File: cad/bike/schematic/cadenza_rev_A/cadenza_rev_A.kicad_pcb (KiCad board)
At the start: 2 copper layers, 80 x 50 mm, 35 parts, among them J2 USB_C_Receptacle, J3 Conn_01x02, Q1 BC547, U1 TLC5916, U10 HDSP-A151, U11 TLC5916, U12 HDSP-A151, U13 STM32F105RCTx, U14 INA193, U15 TLC5916, U2 HDSP-A151, U3 TLC5916, U4 HDSP-A151, U5 TLC5916, U6 HDSP-A151, U7 TLC5916, U8 HDSP-A151, U9 TLC5916

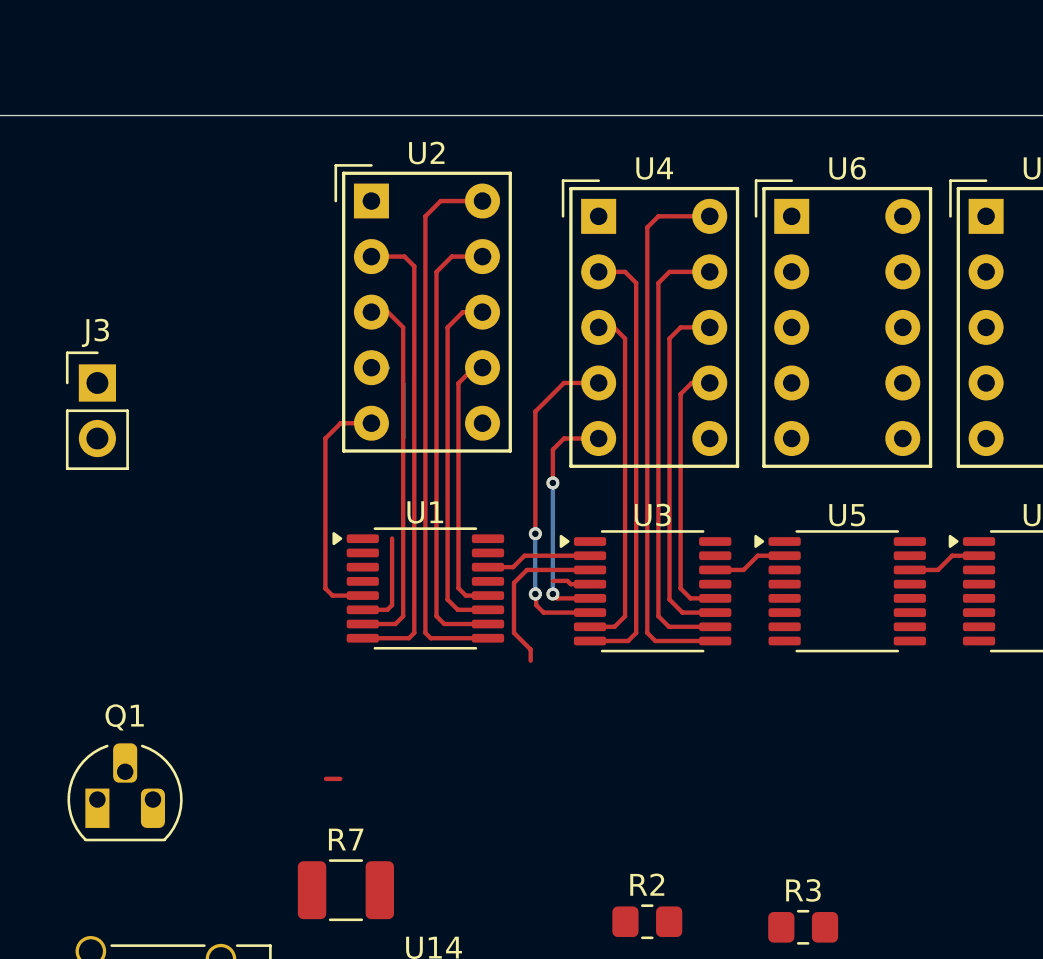
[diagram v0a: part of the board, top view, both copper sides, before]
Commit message: new placement for the LED chips
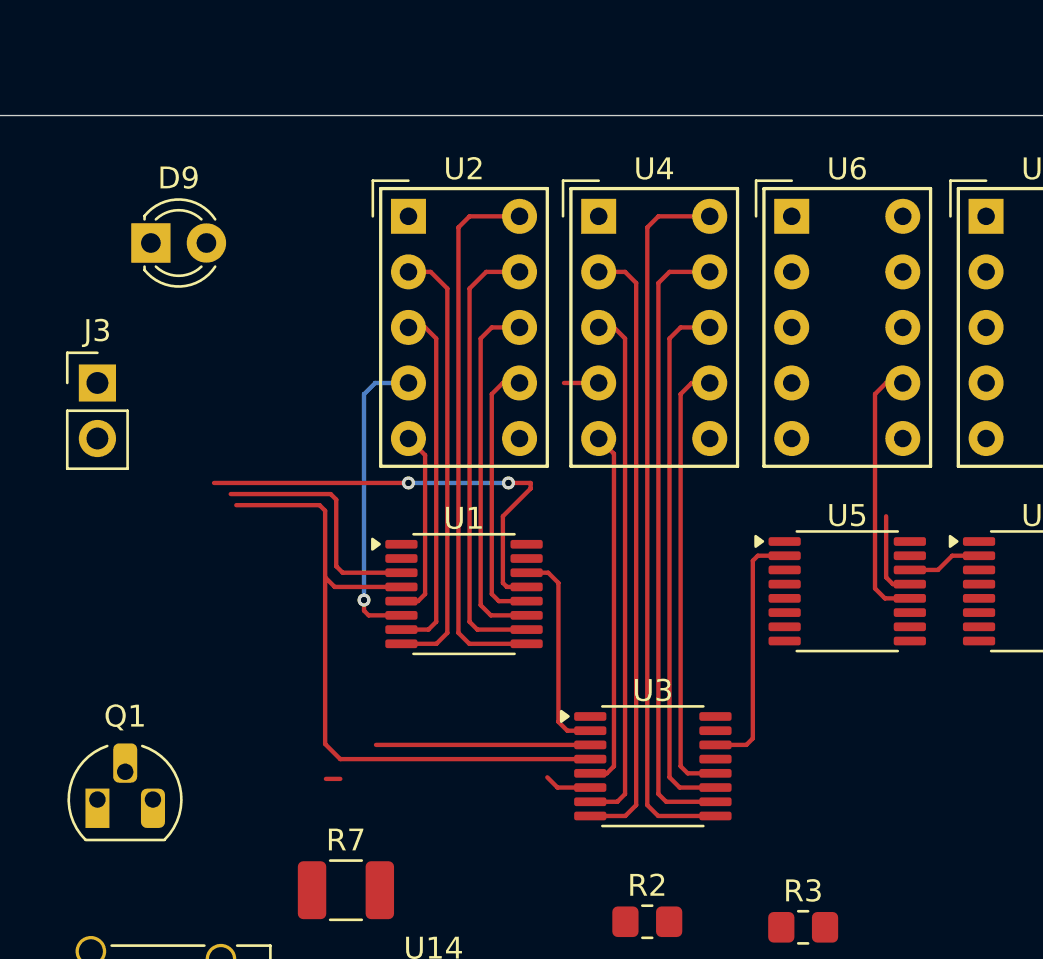
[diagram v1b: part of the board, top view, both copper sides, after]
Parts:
- added D9: LED, LED_THT:LED_D3.0mm, F.Cu at (57.1, 55.8)
- moved U3 8.00 mm to (80.0, 79.8)
- moved U2 1.83 mm to (68.8, 54.6)
- moved U1 1.78 mm to (71.4, 71.9)
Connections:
- U5 pad 10: unconnected-(U5-~{OUT5}-Pad10) -> Net-(U5-~{OUT5})
- U5 pad 11: unconnected-(U5-~{OUT6}-Pad11) -> Net-(U5-~{OUT6})
- U5 pad 12: unconnected-(U5-~{OUT7}-Pad12) -> Net-(U5-~{OUT7})
- U6 pad 7: unconnected-(U6-DP-Pad7) -> Net-(U5-~{OUT7})
- U6 pad 8: unconnected-(U6-C-Pad8) -> Net-(U5-~{OUT6})
- U6 pad 9: unconnected-(U6-B-Pad9) -> Net-(U5-~{OUT5})
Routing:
- net Net-(U1-LE(ED1)): track 1.76 -> 30.9 mm
- net Net-(U1-~{OE}(ED2)): track 0.00 -> 24.7 mm, vias 0 -> 2
- net Net-(U1-CLK): track 7.60 -> 20.9 mm
- net Net-(U5-~{OUT7}): track 0.00 -> 12.2 mm
- net Net-(U3-~{OUT1}): track 15.0 -> 3.74 mm, vias 2 -> 0
- net Net-(U3-~{OUT7}): track 12.2 -> 20.3 mm
- net Net-(U3-~{OUT5}): track 20.6 -> 28.7 mm
- net Net-(U3-~{OUT6}): track 16.3 -> 24.4 mm
- net Net-(U3-~{OUT2}): track 15.9 -> 24.0 mm
- net Net-(U3-SDO): track 3.44 -> 11.5 mm
- net Net-(U3-~{OUT4}): track 24.9 -> 32.8 mm
- net Net-(U3-~{OUT3}): track 20.2 -> 28.1 mm
- net Net-(U1-~{OUT1}): track 7.77 -> 13.9 mm, vias 0 -> 1
- net Net-(U3-~{OUT0}): track 10.7 -> 16.5 mm, vias 2 -> 0
- net Net-(U1-SDO): track 4.88 -> 9.62 mm
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
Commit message: routing progress update
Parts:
- added C3: 100nF, Capacitor_SMD:C_0805_2012Metric_Pad1.18x1.45mm_HandSolder, F.Cu at (77.0, 71.2)
- added C4: 100nF, Capacitor_SMD:C_0805_2012Metric_Pad1.18x1.45mm_HandSolder, F.Cu at (83.1, 74.9)
- added C5: 100nF, Capacitor_SMD:C_0805_2012Metric_Pad1.18x1.45mm_HandSolder, F.Cu at (94.2, 70.9)
- added C6: 100nF, Capacitor_SMD:C_0805_2012Metric_Pad1.18x1.45mm_HandSolder, F.Cu at (100.8, 74.9)
- added R10: R_US, Resistor_SMD:R_0805_2012Metric_Pad1.20x1.40mm_HandSolder, F.Cu at (102.4, 92.7)
- added R8: R_US, Resistor_SMD:R_0805_2012Metric_Pad1.20x1.40mm_HandSolder, F.Cu at (96.6, 87.3)
- added R9: R_US, Resistor_SMD:R_0805_2012Metric_Pad1.20x1.40mm_HandSolder, F.Cu at (91.2, 93.2)
- moved U15 87.8 mm to (116.5, 79.1)
- moved R1 32.0 mm to (71.4, 76.2), turned to 180 degrees
- moved R2 9.66 mm to (87.6, 81.3)
- moved U7 8.00 mm to (97.8, 79.8)
- moved R4 4.66 mm to (108.7, 78.5)
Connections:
- U1 pad 2: unconnected-(U1-SDI-Pad2) -> Net-(U1-SDI)
- U11 pad 15: unconnected-(U11-R-EXT-Pad15) -> Net-(U11-R-EXT)
- U13 pad 14: unconnected-(U13-PA0-Pad14) -> Net-(U1-SDI)
- U5 pad 5: unconnected-(U5-~{OUT0}-Pad5) -> Net-(U5-~{OUT0})
- U5 pad 6: unconnected-(U5-~{OUT1}-Pad6) -> Net-(U5-~{OUT1})
- U5 pad 7: unconnected-(U5-~{OUT2}-Pad7) -> Net-(U5-~{OUT2})
- U5 pad 8: unconnected-(U5-~{OUT3}-Pad8) -> Net-(U5-~{OUT3})
- U5 pad 9: unconnected-(U5-~{OUT4}-Pad9) -> Net-(U5-~{OUT4})
- U6 pad 10: unconnected-(U6-A-Pad10) -> Net-(U5-~{OUT4})
- U6 pad 2: unconnected-(U6-F-Pad2) -> Net-(U5-~{OUT3})
- U6 pad 3: unconnected-(U6-G-Pad3) -> Net-(U5-~{OUT2})
- U6 pad 4: unconnected-(U6-E-Pad4) -> Net-(U5-~{OUT1})
- U6 pad 5: unconnected-(U6-D-Pad5) -> Net-(U5-~{OUT0})
- U7 pad 10: unconnected-(U7-~{OUT5}-Pad10) -> Net-(U7-~{OUT5})
- U7 pad 11: unconnected-(U7-~{OUT6}-Pad11) -> Net-(U7-~{OUT6})
- U7 pad 12: unconnected-(U7-~{OUT7}-Pad12) -> Net-(U7-~{OUT7})
- U7 pad 15: unconnected-(U7-R-EXT-Pad15) -> Net-(U7-R-EXT)
- U7 pad 5: unconnected-(U7-~{OUT0}-Pad5) -> Net-(U7-~{OUT0})
- U7 pad 6: unconnected-(U7-~{OUT1}-Pad6) -> Net-(U7-~{OUT1})
- U7 pad 7: unconnected-(U7-~{OUT2}-Pad7) -> Net-(U7-~{OUT2})
- U7 pad 8: unconnected-(U7-~{OUT3}-Pad8) -> Net-(U7-~{OUT3})
- U7 pad 9: unconnected-(U7-~{OUT4}-Pad9) -> Net-(U7-~{OUT4})
- U8 pad 10: unconnected-(U8-A-Pad10) -> Net-(U7-~{OUT4})
- U8 pad 2: unconnected-(U8-F-Pad2) -> Net-(U7-~{OUT3})
- U8 pad 3: unconnected-(U8-G-Pad3) -> Net-(U7-~{OUT2})
- U8 pad 4: unconnected-(U8-E-Pad4) -> Net-(U7-~{OUT1})
- U8 pad 5: unconnected-(U8-D-Pad5) -> Net-(U7-~{OUT0})
- U8 pad 7: unconnected-(U8-DP-Pad7) -> Net-(U7-~{OUT7})
- U8 pad 8: unconnected-(U8-C-Pad8) -> Net-(U7-~{OUT6})
- U8 pad 9: unconnected-(U8-B-Pad9) -> Net-(U7-~{OUT5})
- U9 pad 15: unconnected-(U9-R-EXT-Pad15) -> Net-(U9-R-EXT)
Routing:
- net +5VL: track 0.00 -> 195.5 mm
- net Net-(U1-CLK): track 20.9 -> 65.1 mm, vias 0 -> 5
- net Net-(U7-~{OUT4}): track 0.00 -> 32.7 mm
- net Net-(U7-~{OUT5}): track 0.00 -> 28.6 mm
- net Net-(U7-~{OUT3}): track 0.00 -> 28.2 mm
- net Net-(U1-~{OE}(ED2)): track 24.7 -> 52.6 mm, vias 2 -> 6
- net Net-(U5-~{OUT4}): track 0.00 -> 24.8 mm
- net Net-(U7-~{OUT6}): track 0.00 -> 24.3 mm
- net Net-(U7-~{OUT2}): track 0.00 -> 24.0 mm
- net +3.3V: track 0.00 -> 21.8 mm, vias 0 -> 1
- net Net-(U5-~{OUT5}): track 0.00 -> 20.7 mm
- net Net-(U5-~{OUT3}): track 0.00 -> 20.2 mm
- net Net-(U7-~{OUT7}): track 0.00 -> 20.1 mm
- net Net-(U3-~{OUT1}): track 3.74 -> 21.4 mm, vias 0 -> 2
- net Net-(U7-~{OUT0}): track 0.00 -> 16.5 mm
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
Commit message: routing progress update
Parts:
- added C7: 100nF, Capacitor_SMD:C_0805_2012Metric_Pad1.18x1.45mm_HandSolder, F.Cu at (118.6, 74.9)
- added C8: 100nF, Capacitor_SMD:C_0805_2012Metric_Pad1.18x1.45mm_HandSolder, F.Cu at (112.0, 70.9)
- moved R4 55.5 mm to (53.3, 74.2), turned to 180 degrees
- moved R9 23.0 mm to (106.7, 76.2), turned to 180 degrees
- moved U13 18.1 mm to (95.0, 93.2)
- moved R10 15.8 mm to (115.6, 84.1), turned to 180 degrees
- moved U15 14.2 mm to (116.6, 93.2)
- moved R3 11.1 mm to (88.9, 76.2), turned to 180 degrees
- moved R2 8.12 mm to (80.0, 84.1), turned to 180 degrees
- moved U11 8.00 mm to (115.6, 79.8)
- moved R8 3.47 mm to (97.8, 84.1), turned to 180 degrees
- moved C3 0.45 mm to (76.7, 70.9)
- moved U5 0.13 mm to (88.9, 71.9)
- moved U9 0.13 mm to (106.7, 71.9)
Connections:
- C6 pad 1: unconnected-(C6-Pad1) -> GND
- U10 pad 10: unconnected-(U10-A-Pad10) -> Net-(U10-A)
- U10 pad 2: unconnected-(U10-F-Pad2) -> Net-(U10-F)
- U10 pad 3: unconnected-(U10-G-Pad3) -> Net-(U10-G)
- U10 pad 4: unconnected-(U10-E-Pad4) -> Net-(U10-E)
- U10 pad 5: unconnected-(U10-D-Pad5) -> Net-(U10-D)
- U10 pad 7: unconnected-(U10-DP-Pad7) -> Net-(U10-DP)
- U10 pad 8: unconnected-(U10-C-Pad8) -> Net-(U10-C)
- U10 pad 9: unconnected-(U10-B-Pad9) -> Net-(U10-B)
- U11 pad 10: unconnected-(U11-~{OUT5}-Pad10) -> Net-(U11-~{OUT5})
- U11 pad 11: unconnected-(U11-~{OUT6}-Pad11) -> Net-(U11-~{OUT6})
- U11 pad 12: unconnected-(U11-~{OUT7}-Pad12) -> Net-(U11-~{OUT7})
- U11 pad 5: unconnected-(U11-~{OUT0}-Pad5) -> Net-(U11-~{OUT0})
- U11 pad 6: unconnected-(U11-~{OUT1}-Pad6) -> Net-(U11-~{OUT1})
- U11 pad 7: unconnected-(U11-~{OUT2}-Pad7) -> Net-(U11-~{OUT2})
- U11 pad 8: unconnected-(U11-~{OUT3}-Pad8) -> Net-(U11-~{OUT3})
- U11 pad 9: unconnected-(U11-~{OUT4}-Pad9) -> Net-(U11-~{OUT4})
- U12 pad 10: unconnected-(U12-A-Pad10) -> Net-(U11-~{OUT4})
- U12 pad 2: unconnected-(U12-F-Pad2) -> Net-(U11-~{OUT3})
- U12 pad 3: unconnected-(U12-G-Pad3) -> Net-(U11-~{OUT2})
- U12 pad 4: unconnected-(U12-E-Pad4) -> Net-(U11-~{OUT1})
- U12 pad 5: unconnected-(U12-D-Pad5) -> Net-(U11-~{OUT0})
- U12 pad 7: unconnected-(U12-DP-Pad7) -> Net-(U11-~{OUT7})
- U12 pad 8: unconnected-(U12-C-Pad8) -> Net-(U11-~{OUT6})
- U12 pad 9: unconnected-(U12-B-Pad9) -> Net-(U11-~{OUT5})
- U9 pad 10: unconnected-(U9-~{OUT5}-Pad10) -> Net-(U10-B)
- U9 pad 11: unconnected-(U9-~{OUT6}-Pad11) -> Net-(U10-C)
- U9 pad 12: unconnected-(U9-~{OUT7}-Pad12) -> Net-(U10-DP)
- U9 pad 5: unconnected-(U9-~{OUT0}-Pad5) -> Net-(U10-D)
- U9 pad 6: unconnected-(U9-~{OUT1}-Pad6) -> Net-(U10-E)
- U9 pad 7: unconnected-(U9-~{OUT2}-Pad7) -> Net-(U10-G)
- U9 pad 8: unconnected-(U9-~{OUT3}-Pad8) -> Net-(U10-F)
- U9 pad 9: unconnected-(U9-~{OUT4}-Pad9) -> Net-(U10-A)
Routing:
- net Net-(U1-LE(ED1)): track 19.9 -> 65.5 mm, vias 0 -> 2
- net +3.3V: track 21.8 -> 64.3 mm, vias 1 -> 5
- net Net-(U1-CLK): track 65.1 -> 102.9 mm, vias 5 -> 10
- net Net-(U11-~{OUT4}): track 0.00 -> 32.7 mm
- net Net-(U11-~{OUT5}): track 0.00 -> 28.6 mm
- net Net-(U11-~{OUT3}): track 0.00 -> 28.2 mm
- net Net-(U7-~{OUT1}): track 0.00 -> 26.6 mm, vias 0 -> 1
- net Net-(U11-~{OUT1}): track 0.00 -> 25.6 mm, vias 0 -> 1
- net Net-(U10-A): track 0.00 -> 24.9 mm
- net Net-(U11-~{OUT6}): track 0.00 -> 24.3 mm
- net Net-(U11-~{OUT2}): track 0.00 -> 24.0 mm
- net Net-(U10-B): track 0.00 -> 20.7 mm
- net Net-(U10-F): track 0.00 -> 20.3 mm
- net Net-(U11-~{OUT7}): track 0.00 -> 20.2 mm
- net Net-(U10-C): track 0.00 -> 16.6 mm
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
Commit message: added the SPI interface
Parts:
- added C10: 100nF, Capacitor_SMD:C_0805_2012Metric_Pad1.18x1.45mm_HandSolder, F.Cu at (81.4, 92.9)
- added C11: 100nF, Capacitor_SMD:C_0805_2012Metric_Pad1.18x1.45mm_HandSolder, F.Cu at (81.4, 95.9)
- added C9: 100nF, Capacitor_SMD:C_0805_2012Metric_Pad1.18x1.45mm_HandSolder, F.Cu at (81.4, 89.9)
- moved U13 1.63 mm to (93.7, 92.2), turned to -90 degrees
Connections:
- U1 pad 2: Net-(U1-SDI) -> /SPI_MOSI
- U1 pad 3: Net-(U1-CLK) -> /SPI_CLK
- U11 pad 3: Net-(U1-CLK) -> /SPI_CLK
- U13 pad 14: Net-(U1-SDI) -> unconnected-(U13-PA0-Pad14)
- U13 pad 21: unconnected-(U13-PA5-Pad21) -> /SPI_CLK
- U13 pad 22: unconnected-(U13-PA6-Pad22) -> /SPI_MISO
- U13 pad 23: unconnected-(U13-PA7-Pad23) -> /SPI_MOSI
- U15 pad 3: Net-(U1-CLK) -> /SPI_CLK
- U3 pad 3: Net-(U1-CLK) -> /SPI_CLK
- U5 pad 3: Net-(U1-CLK) -> /SPI_CLK
- U7 pad 3: Net-(U1-CLK) -> /SPI_CLK
- U9 pad 3: Net-(U1-CLK) -> /SPI_CLK
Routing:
- net Net-(U1-CLK): track 102.9 -> 0.00 mm, vias 10 -> 0
- net /SPI_CLK: track 0.00 -> 102.9 mm, vias 0 -> 10
- net Net-(U1-SDI): track 2.32 -> 0.00 mm
- net /SPI_MOSI: track 0.00 -> 2.32 mm

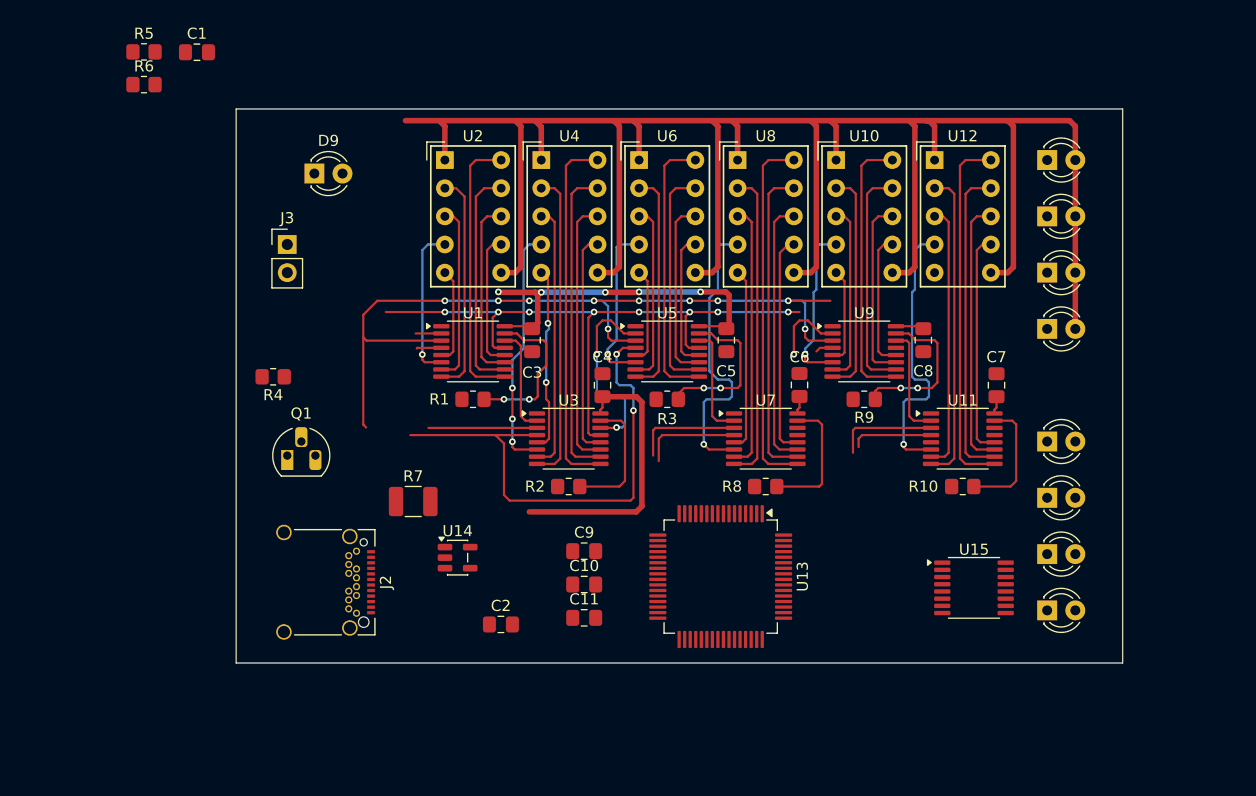
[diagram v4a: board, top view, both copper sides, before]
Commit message: added routing for the acceleration LEDs
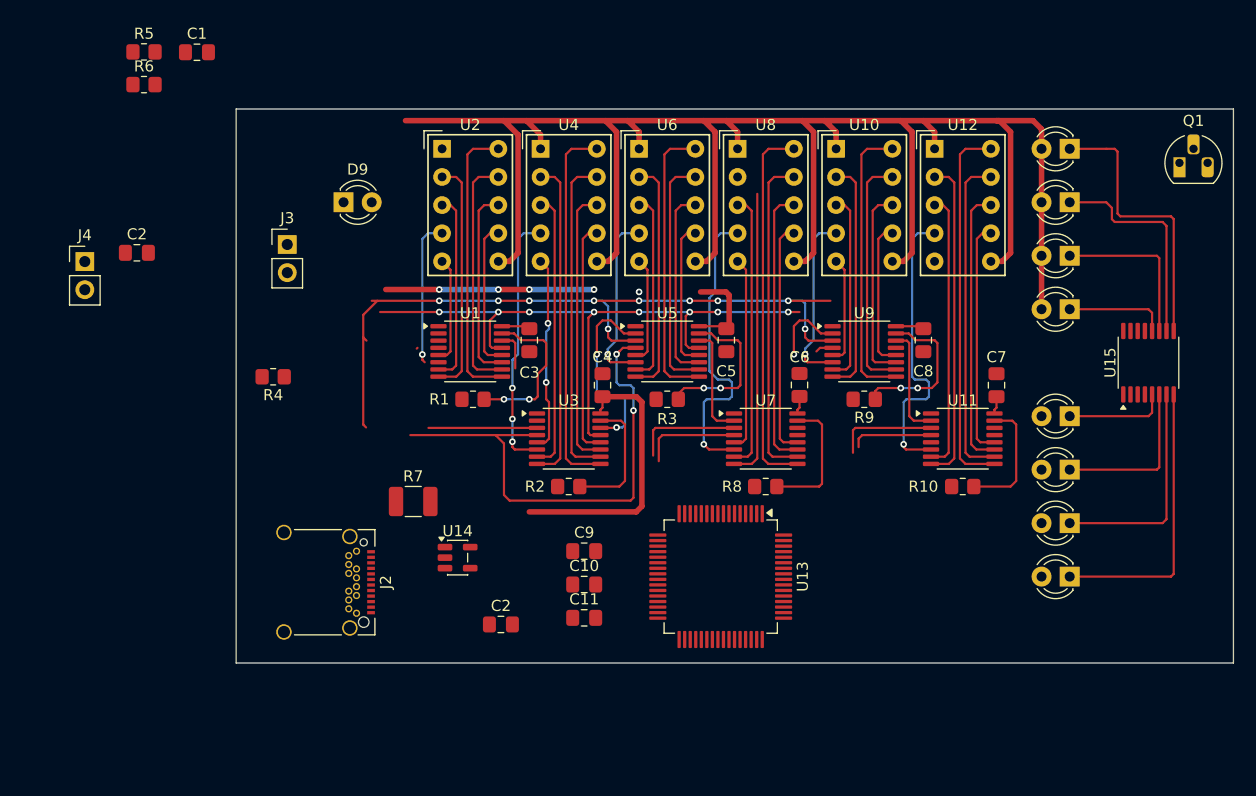
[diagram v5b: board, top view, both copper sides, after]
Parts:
- added C2: 100nF, Capacitor_SMD:C_0805_2012Metric_Pad1.18x1.45mm_HandSolder, F.Cu at (41.0, 63.0)
- added J4: Conn_01x02, Connector_PinHeader_2.54mm:PinHeader_1x02_P2.54mm_Vertical, F.Cu at (36.3, 63.8)
- moved Q1 84.7 mm to (135.1, 54.9)
- moved U15 25.7 mm to (132.3, 72.9), turned to 90 degrees
- moved D9 3.70 mm to (59.7, 58.4)
- moved D8 3.66 mm to (125.2, 92.2), turned to 180 degrees
- moved D7 3.45 mm to (125.2, 87.4), turned to 180 degrees
- moved D6 3.25 mm to (125.2, 82.5), turned to 180 degrees
- moved D5 3.06 mm to (125.2, 77.7), turned to 180 degrees
- moved D4 2.70 mm to (125.2, 68.1), turned to 180 degrees
- moved D3 2.54 mm to (125.2, 63.2), turned to 180 degrees
- moved D2 2.40 mm to (125.2, 58.4), turned to 180 degrees
- moved D1 2.27 mm to (125.2, 53.6), turned to 180 degrees
- moved U2 1.05 mm to (68.6, 53.6)
- moved U4 1.02 mm to (77.5, 53.6)
- moved U10 1.02 mm to (104.1, 53.6)
- moved U12 1.02 mm to (113.0, 53.6)
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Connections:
- J2 pad A4: Net-(U14-+) -> Net-(J4-Pin_1)
- J2 pad A9: Net-(U14-+) -> Net-(J4-Pin_1)
- J2 pad B4: Net-(U14-+) -> Net-(J4-Pin_1)
- J2 pad B9: Net-(U14-+) -> Net-(J4-Pin_1)
- U15 pad 10: Net-(D6-K) -> Net-(D2-K)
- U15 pad 11: Net-(D7-K) -> Net-(D3-K)
- U15 pad 12: Net-(D8-K) -> Net-(D4-K)
- U15 pad 14: unconnected-(U15-SDO-Pad14) -> /SPI_MISO
- U15 pad 5: Net-(D1-K) -> Net-(D5-K)
- U15 pad 6: Net-(D2-K) -> Net-(D6-K)
- U15 pad 7: Net-(D3-K) -> Net-(D7-K)
- U15 pad 8: Net-(D4-K) -> Net-(D8-K)
- U15 pad 9: Net-(D5-K) -> Net-(D1-K)
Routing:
- net Net-(D8-K): track 0.00 -> 25.7 mm
- net Net-(D1-K): track 0.00 -> 25.4 mm
- net +3.3V: track 64.3 -> 42.7 mm, vias 5 -> 1
- net Net-(D7-K): track 0.00 -> 20.1 mm
- net Net-(D2-K): track 0.00 -> 19.7 mm
- net +5VL: track 195.5 -> 176.0 mm
- net (no net): track 0.00 -> 18.8 mm, vias 0 -> 4
- net Net-(D6-K): track 0.00 -> 14.8 mm
- net Net-(D3-K): track 0.00 -> 14.8 mm
- net Net-(D5-K): track 0.00 -> 9.21 mm
- net Net-(D4-K): track 0.00 -> 9.21 mm
- net /SPI_CLK: track 102.9 -> 96.7 mm
- net Net-(U1-SDO): track 9.62 -> 3.58 mm
- net /SPI_MOSI: track 2.32 -> 0.00 mm
- net Net-(U1-LE(ED1)): track 65.5 -> 63.4 mm
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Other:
- board size 80 x 50 mm -> 90 x 50 mm

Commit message: routing progress update
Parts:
- added C12: 100nF, Capacitor_SMD:C_0805_2012Metric_Pad1.18x1.45mm_HandSolder, F.Cu at (124.5, 72.4)
- moved R6 89.6 mm to (129.3, 66.5), turned to 180 degrees
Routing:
- net +5VL: track 176.0 -> 200.1 mm
- net Net-(D4-K): track 9.21 -> 1.64 mm
